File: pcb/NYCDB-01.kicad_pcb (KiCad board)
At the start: 2 copper layers, 263 parts, among them J1 AUDIO_JACK, J2 AUDIO_JACK, P1 CONN_BATT, P2 USB_OTG, Q1 Q_PMOS_GSD, SW1 SW_POWER, SW2 SW_RESET, U1 CS5361, U10 OPA4134, U11 TPA6120A2, U12 24C16, U13 M25P40, U14 XC6SLX9TQG144, U15 LT1086CT-12, U16 LT1086CT-5, U17 LT3015ET-ADJ, U18 LT3015ET-ADJ, U2 OP1642, U3 OP1642, U4 93CxxA, U5 FT2232D, U6 bq2409x, U7 LTC3521, U8 LT3579, U9 PCM1792A, X1 6MHz, X2 12.288MHz, X3 12.288MHz, X4 12.288MHz

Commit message: Still fixing errors
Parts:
- moved C83 1.27 mm to (124.5, 86.4)
- moved C4 0.72 mm to (94.0, 125.7)
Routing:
- net +3V3: track 479.5 -> 455.2 mm
- net /CS5361 ADC/ADC_OVFL: track 28.7 -> 11.5 mm
- net Net-(C1-Pad1): track 20.6 -> 24.5 mm
- net GND: track 169.1 -> 172.1 mm, vias 106 -> 108
- net /CS5361 ADC/left buffer/VQ: track 112.5 -> 114.6 mm

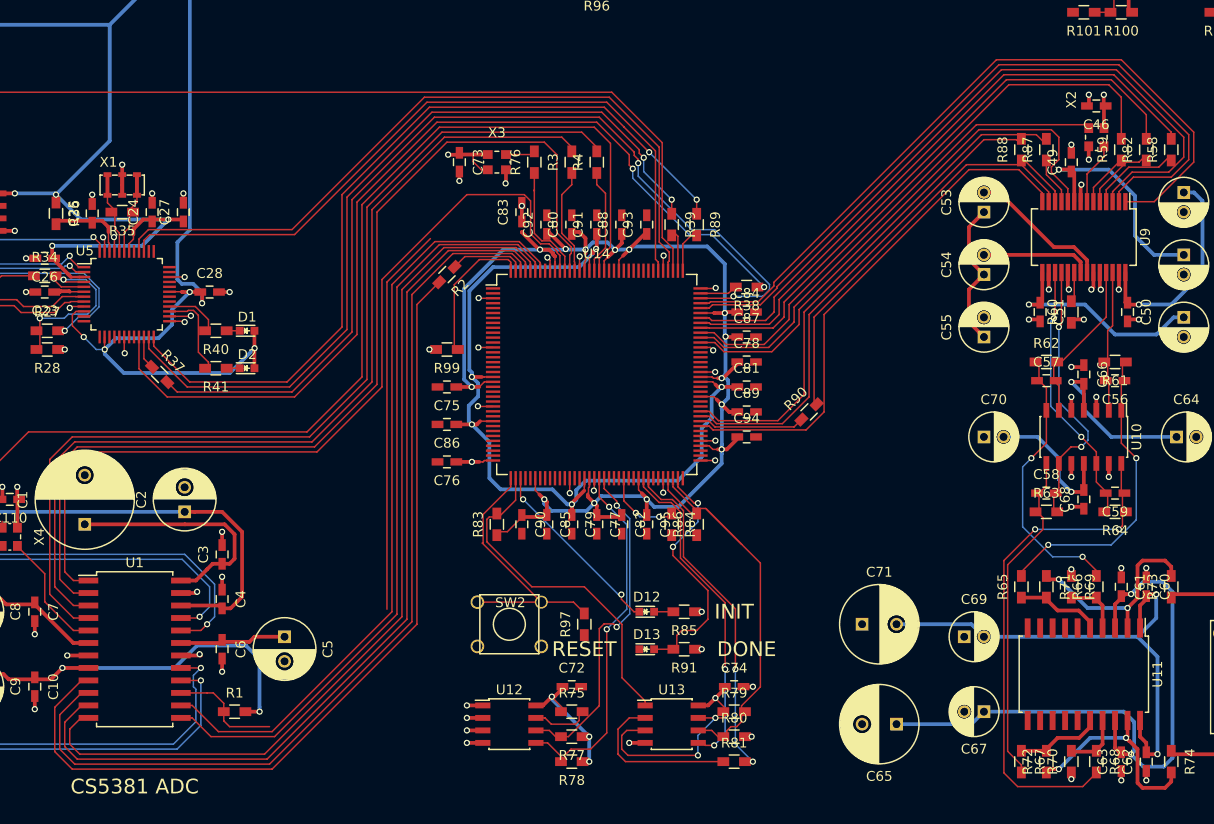
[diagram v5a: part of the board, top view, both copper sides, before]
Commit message: Cleaned up most of the FPGA errors
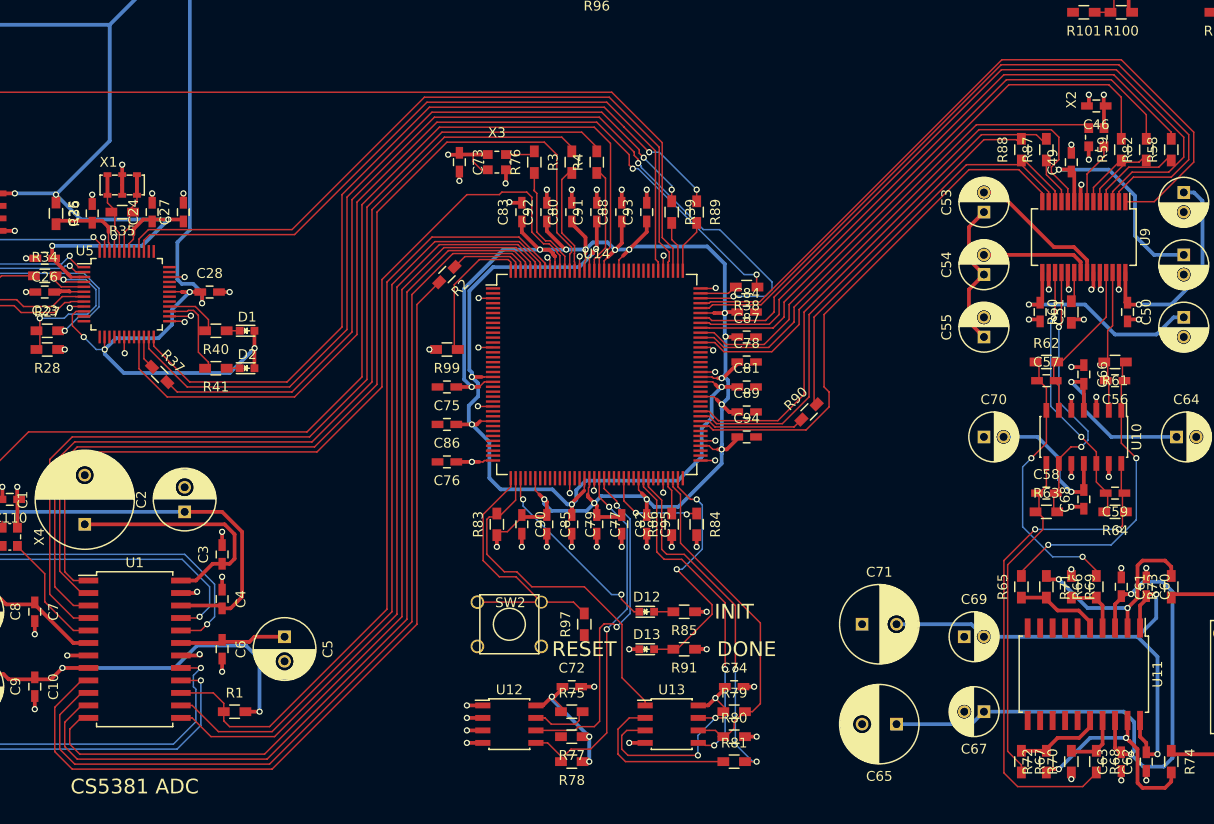
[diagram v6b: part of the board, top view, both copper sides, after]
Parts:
- moved R84 2.54 mm to (142.2, 118.1)
- moved R86 2.54 mm to (139.7, 118.1)
- moved C80 1.27 mm to (129.5, 86.4)
- moved C88 1.27 mm to (134.6, 86.4)
- moved C91 1.27 mm to (132.1, 86.4)
- moved C92 1.27 mm to (127.0, 86.4)
- moved C93 1.27 mm to (137.2, 86.4)
- moved R39 1.27 mm to (139.7, 86.4)
- moved R89 1.27 mm to (142.2, 86.4)
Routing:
- net /CS5361 ADC/ADC_OVFL: track 11.5 -> 81.5 mm
- net +3V3: track 455.2 -> 423.9 mm, vias 36 -> 38
- net GND: track 172.1 -> 190.8 mm, vias 108 -> 122
- net Net-(R86-Pad2): track 9.51 -> 3.74 mm
- net Net-(R84-Pad1): track 7.85 -> 10.3 mm
- net /FT2232D/TMS: track 96.6 -> 95.1 mm
- net /FT2232D/TDI: track 81.9 -> 80.7 mm
- net +1V2: track 104.7 -> 105.8 mm
- net Net-(R39-Pad2): track 4.32 -> 5.32 mm
- net Net-(R97-Pad2): track 28.1 -> 28.9 mm
- net Net-(R89-Pad2): track 4.64 -> 5.44 mm
- net Net-(R81-Pad2): track 35.0 -> 35.8 mm
- net Net-(R83-Pad2): track 34.7 -> 35.4 mm

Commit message: Cleaning up FT2232D
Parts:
- moved R41 4.49 mm to (92.7, 97.8)
- moved D2 4.44 mm to (96.5, 97.8)
- moved R40 3.24 mm to (92.7, 95.2)
- moved D1 3.17 mm to (96.5, 95.2)
- moved R33 2.29 mm to (61.0, 83.8)
- moved R28 1.80 mm to (74.9, 101.6)
- moved R31 1.80 mm to (61.0, 86.4)
- moved C28 1.78 mm to (92.7, 92.7)
- moved R27 1.42 mm to (74.9, 99.1)
- moved R32 1.42 mm to (61.0, 88.9)
- moved C26 1.35 mm to (74.9, 90.2)
- moved C23 1.27 mm to (74.9, 95.2)
- moved R34 1.02 mm to (74.9, 92.7)
- moved C27 0.13 mm to (90.2, 86.4)
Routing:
- net /FT2232D/USB5V: track 119.3 -> 111.4 mm
- net +3V3: track 423.9 -> 417.9 mm, vias 38 -> 37
- net Net-(R41-Pad2): track 9.00 -> 3.53 mm
- net Net-(R33-Pad1): track 23.9 -> 18.7 mm, vias 2 -> 1
- net Net-(R31-Pad2): track 5.87 -> 1.83 mm
- net Net-(R40-Pad2): track 5.65 -> 3.28 mm
- net Net-(R27-Pad1): track 17.0 -> 15.0 mm
- net Net-(R31-Pad1): track 21.3 -> 19.4 mm, vias 2 -> 1
- net +5V: track 223.8 -> 225.2 mm, vias 12 -> 11
- net Net-(C23-Pad1): track 3.29 -> 4.38 mm
- net /FT2232D/USBD-: track 11.0 -> 12.1 mm
- net Net-(U4-Pad1): track 22.3 -> 22.1 mm, vias 2 -> 1
- net GND: vias 122 -> 121

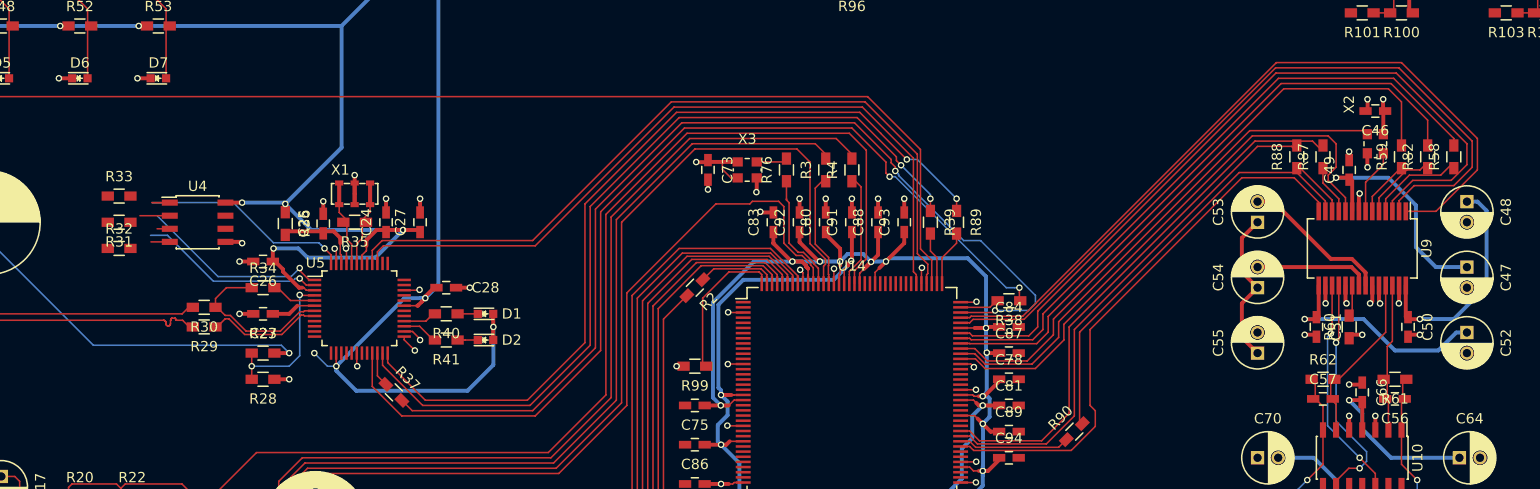
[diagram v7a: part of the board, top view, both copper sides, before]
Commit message: Now cleaning up some of the DAC
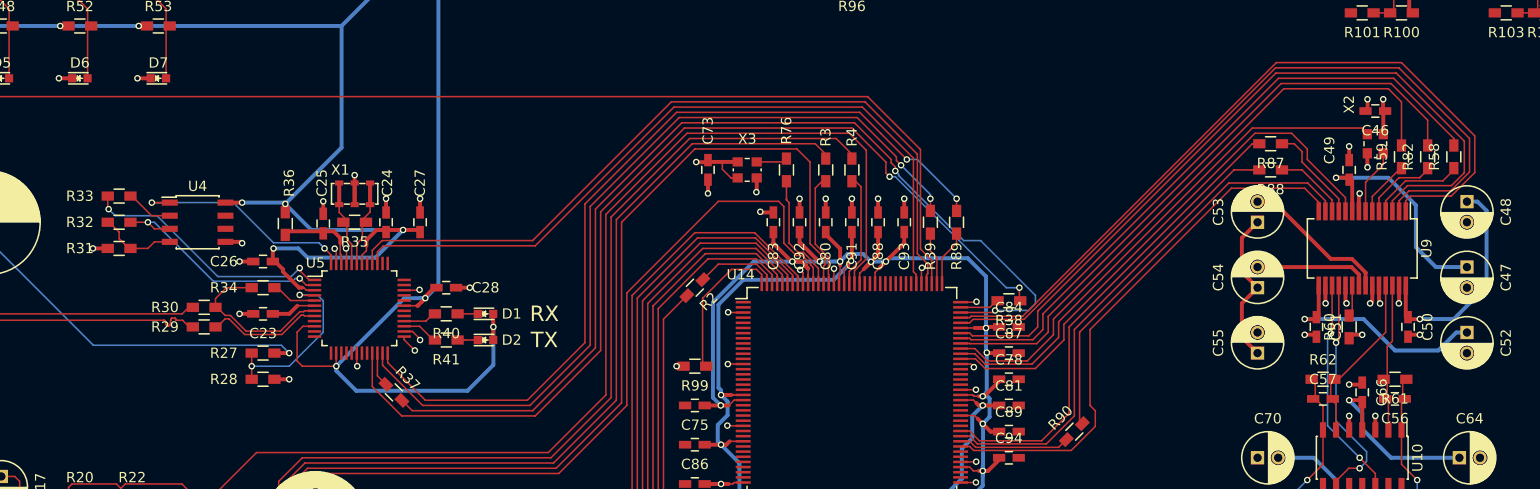
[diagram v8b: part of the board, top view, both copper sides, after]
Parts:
- moved R87 5.24 mm to (172.7, 78.7), turned to 180 degrees
- moved R88 2.84 mm to (172.7, 81.3), turned to 180 degrees
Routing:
- net /TI DAC/DAC_MDO: track 10.1 -> 40.7 mm
- net Net-(R88-Pad1): track 37.4 -> 7.18 mm
- net /TI DAC/DAC_MDI: track 52.8 -> 46.2 mm
- net Net-(R33-Pad1): track 18.7 -> 25.0 mm, vias 1 -> 2
- net +3V3: track 417.9 -> 424.0 mm, vias 37 -> 36
- net Net-(R31-Pad2): track 1.83 -> 7.71 mm
- net /TI DAC/DAC_MC: track 49.9 -> 45.2 mm
- net Net-(R87-Pad1): track 5.18 -> 9.54 mm
- net Net-(R31-Pad1): track 19.4 -> 23.0 mm, vias 1 -> 2
- net Net-(R27-Pad1): track 15.0 -> 17.9 mm
- net /TI DAC/DAC_MS: track 55.0 -> 52.6 mm
- net Net-(R33-Pad2): track 2.90 -> 4.61 mm
- net +5V: track 225.2 -> 226.7 mm, vias 11 -> 12
- net /CS5361 ADC/ADC_OVFL: track 81.5 -> 82.7 mm
- net /CS5361 ADC/ADC_M1: track 79.5 -> 80.7 mm
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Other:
- board text added: "RX"
- board text added: "TX"
